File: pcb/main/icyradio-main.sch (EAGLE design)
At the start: 702 parts, among them CON101 FPC-22P, CON102 FPC-22P, CON1101 2EDG-2P-5MM-H, CON701 4P-SH-TOP, CON801 PCIE-X4-EDGE, J101 RJ45_MAG_LED_1G-TE-1-2301994-0, J701 TRSJACK, J702 TRSJACK, J703 TRSJACK, M701 SPH0641LM4H-1, M702 SPH0641LM4H-1, Q101 AO3400, Q102 AO3400, Q1101 AO3400, Q1102 AO4805, Q1103 AO3400, Q1104 AO4805, Q1105 AO4805, Q1106 AO3400, T501 UWB1-85E, T502 UWB1-85E, T503 UWB1-85E, T504 UWB1-85E, T505 UWB1-85E, T506 UWB1-85E, T507 UWB1-85E, T508 UWB1-85E, U1001 LTC4313-3, U1002 UPD301C, U1003 MIC2019, U101 MIC2019, U102 RPI-CM4, U1101 MCP1804-3302, U1102 LT7182S, U1201 ADM7172ACPZ-5.0, U1202 ADM7171ACPZ-1.3, U1203 ADM7171ACPZ-3.3, U1204 MIC23159, U1205 MIC5166, U1206 ADM7171ACPZ-1.3, U1207 ADM7171ACPZ-3.3, U1208 MIC23159, U1209 MIC23155, U1210 ADP7142AUJZ-3.3, U201 XC7A100TFGG484, U202 SST26VF064B, U301 MT41K256M16TW-125, U401 AD9361, U501 MIC2019, U502 MIC2019, U503 MIC2019, U504 MIC2019, U505 ADL5601, U506 ADL5601, U601 8V97003, U701 ADAU1372, U901 DSB321SDA, U902 SI5351C-B-GM

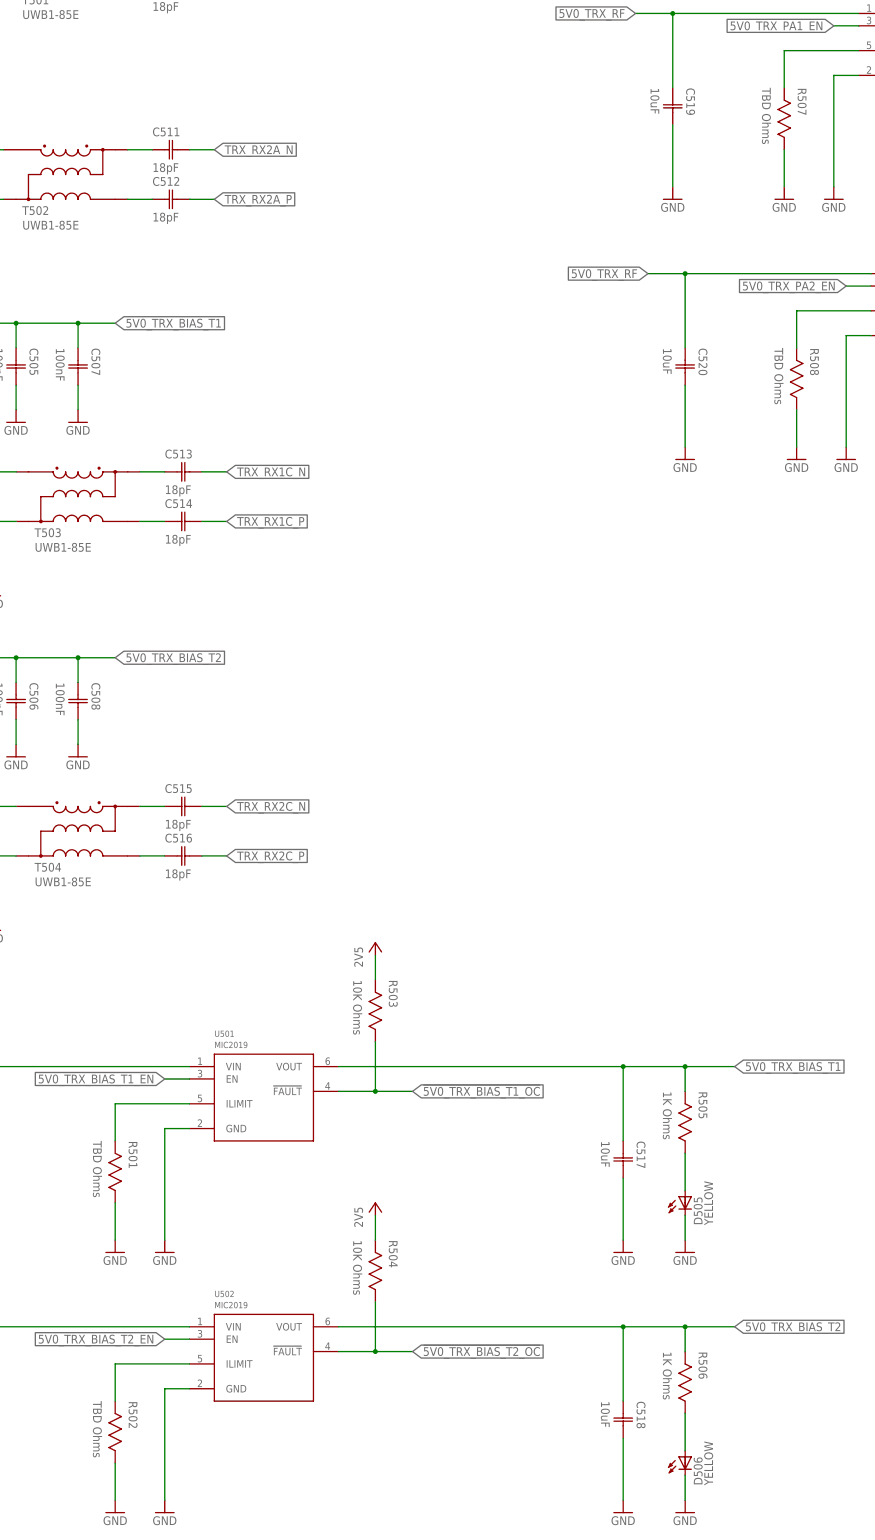
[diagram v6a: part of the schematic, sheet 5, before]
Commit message: Set values for current limit switches Final touches for production Re-generate gerbers, schematic PDF and PCB pictures
Signed-off-by: João Silva <jgc3silva@gmail.com>
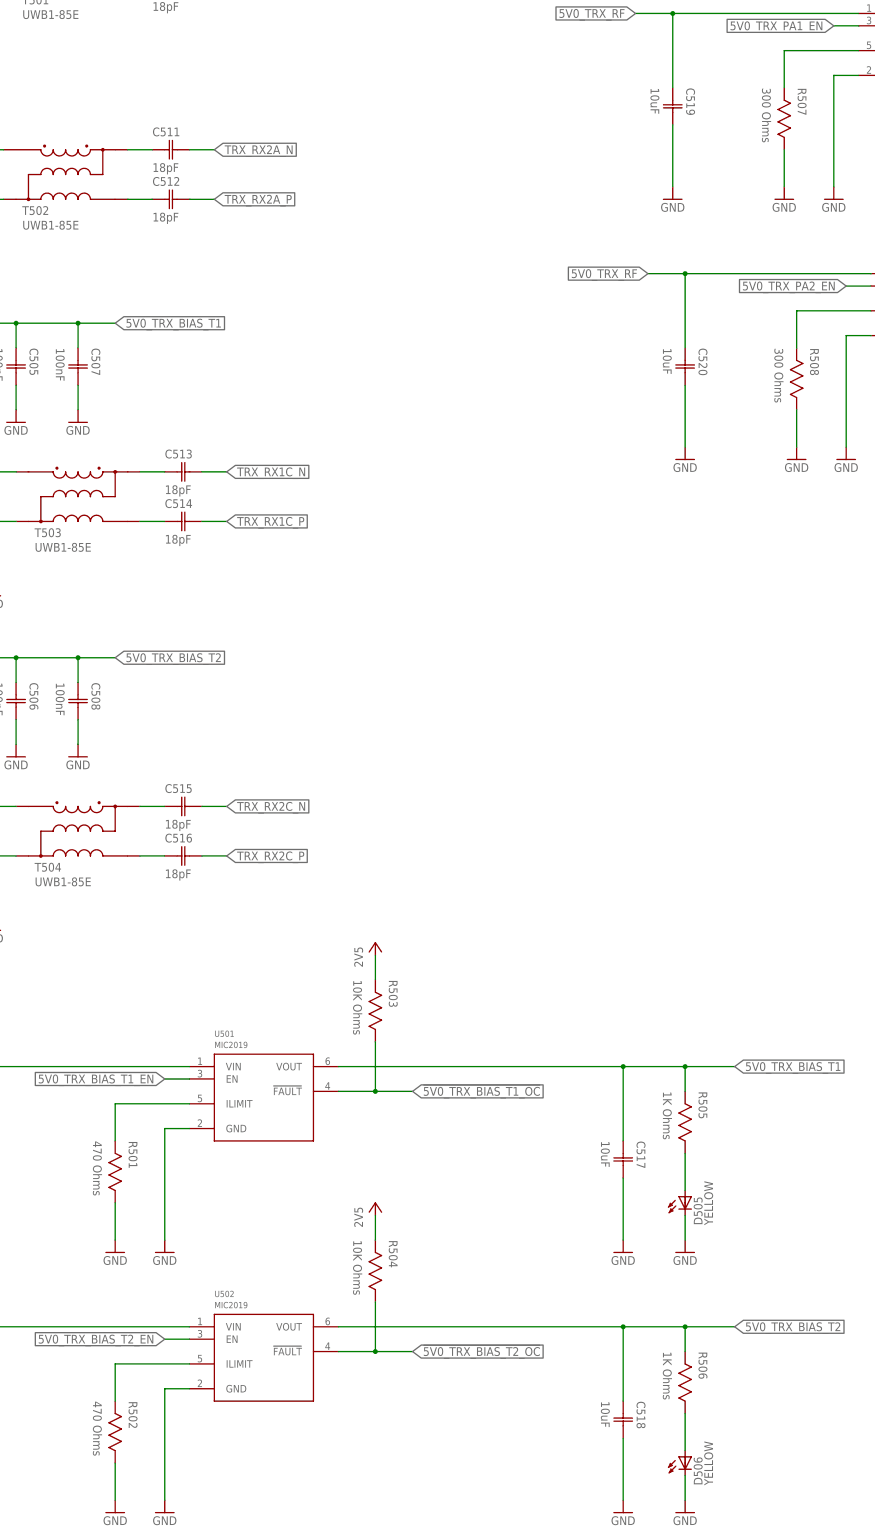
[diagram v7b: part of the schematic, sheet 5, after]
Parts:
- R1010, R501, R502: value TBD Ohms -> 470 Ohms
- R104: value TBD Ohms -> 1.2K Ohms
- R401, R402: value 25 Ohms -> 25.5 Ohms
- R507, R508: value TBD Ohms -> 300 Ohms
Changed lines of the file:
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@@
 <part name="GND72" library="Supply Symbol" deviceset="GND" device=""/>
 <part name="GND73" library="Supply Symbol" deviceset="GND" device=""/>
-<part name="R402" library="Resistor" deviceset="RESISTOR" device="-0402" value="25 Ohms"/>
-<part name="R401" library="Resistor" deviceset="RESISTOR" device="-0402" value="25 Ohms"/>
+<part name="R402" library="Resistor" deviceset="RESISTOR" device="-0402" value="25.5 Ohms"/>
+<part name="R401" library="Resistor" deviceset="RESISTOR" device="-0402" value="25.5 Ohms"/>
 <part name="C711" library="Capacitor" deviceset="CAPACITOR" device="-0402" value="100nF"/>
 <part name="GND74" library="Supply Symbol" deviceset="GND" device=""/>
@@
 <part name="C519" library="Capacitor" deviceset="CAPACITOR" device="-0603" value="10uF"/>
 <part name="GND240" library="Supply Symbol" deviceset="GND" device=""/>
-<part name="R507" library="Resistor" deviceset="RESISTOR" device="-0402" value="TBD Ohms"/>
+<part name="R507" library="Resistor" deviceset="RESISTOR" device="-0402" value="300 Ohms"/>
 <part name="GND241" library="Supply Symbol" deviceset="GND" device=""/>
 <part name="GND250" library="Supply Symbol" deviceset="GND" device=""/>
@@
 <part name="C520" library="Capacitor" deviceset="CAPACITOR" device="-0603" value="10uF"/>
 <part name="GND253" library="Supply Symbol" deviceset="GND" device=""/>
-<part name="R508" library="Resistor" deviceset="RESISTOR" device="-0402" value="TBD Ohms"/>
+<part name="R508" library="Resistor" deviceset="RESISTOR" device="-0402" value="300 Ohms"/>
 <part name="GND254" library="Supply Symbol" deviceset="GND" device=""/>
 <part name="GND255" library="Supply Symbol" deviceset="GND" device=""/>
@@
 <part name="C503" library="Capacitor" deviceset="CAPACITOR" device="-0603" value="10uF"/>
 <part name="GND258" library="Supply Symbol" deviceset="GND" device=""/>
-<part name="R501" library="Resistor" deviceset="RESISTOR" device="-0402" value="TBD Ohms"/>
+<part name="R501" library="Resistor" deviceset="RESISTOR" device="-0402" value="470 Ohms"/>
 <part name="GND259" library="Supply Symbol" deviceset="GND" device=""/>
 <part name="GND260" library="Supply Symbol" deviceset="GND" device=""/>
@@
 <part name="C504" library="Capacitor" deviceset="CAPACITOR" device="-0603" value="10uF"/>
 <part name="GND263" library="Supply Symbol" deviceset="GND" device=""/>
-<part name="R502" library="Resistor" deviceset="RESISTOR" device="-0402" value="TBD Ohms"/>
+<part name="R502" library="Resistor" deviceset="RESISTOR" device="-0402" value="470 Ohms"/>
 <part name="GND264" library="Supply Symbol" deviceset="GND" device=""/>
 <part name="GND265" library="Supply Symbol" deviceset="GND" device=""/>
@@
 <part name="U101" library="Microchip" deviceset="MIC20*9" device="" technology="1"/>
 <part name="GND151" library="Supply Symbol" deviceset="GND" device=""/>
-<part name="R104" library="Resistor" deviceset="RESISTOR" device="-0402" value="TBD Ohms"/>
+<part name="R104" library="Resistor" deviceset="RESISTOR" device="-0402" value="1.2K Ohms"/>
 <part name="GND171" library="Supply Symbol" deviceset="GND" device=""/>
 <part name="C105" library="Capacitor" deviceset="CAPACITOR" device="-0402" value="10uF"/>
@@
 <part name="5V00015" library="Supply Symbol" deviceset="5V0" device=""/>
 <part name="R1009" library="Resistor" deviceset="RESISTOR" device="-0402" value="10K Ohms"/>
-<part name="R1010" library="Resistor" deviceset="RESISTOR" device="-0402" value="TBD Ohms"/>
+<part name="R1010" library="Resistor" deviceset="RESISTOR" device="-0402" value="470 Ohms"/>
 <part name="GND130" library="Supply Symbol" deviceset="GND" device=""/>
 <part name="GND132" library="Supply Symbol" deviceset="GND" device=""/>
